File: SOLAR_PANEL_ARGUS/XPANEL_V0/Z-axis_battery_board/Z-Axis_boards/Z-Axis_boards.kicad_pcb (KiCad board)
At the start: 2 copper layers, 95.9 x 90.2 mm, 34 parts, among them J1 0530470810, Q1 BSS138, Q2 BSS138, Q3 MBT2222ADW1T1, Q4 BSS138, Q5 BSS138, Q6 MBT2222ADW1T1, U1 DRV8830DGQ

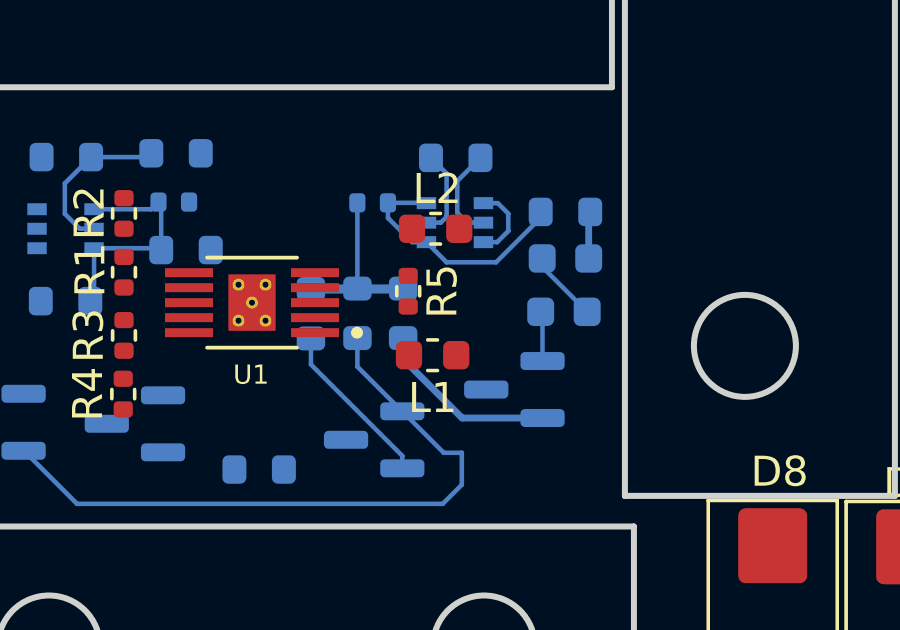
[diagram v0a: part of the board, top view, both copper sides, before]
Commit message: Started intial coil loop on first layer on Z-Axis board
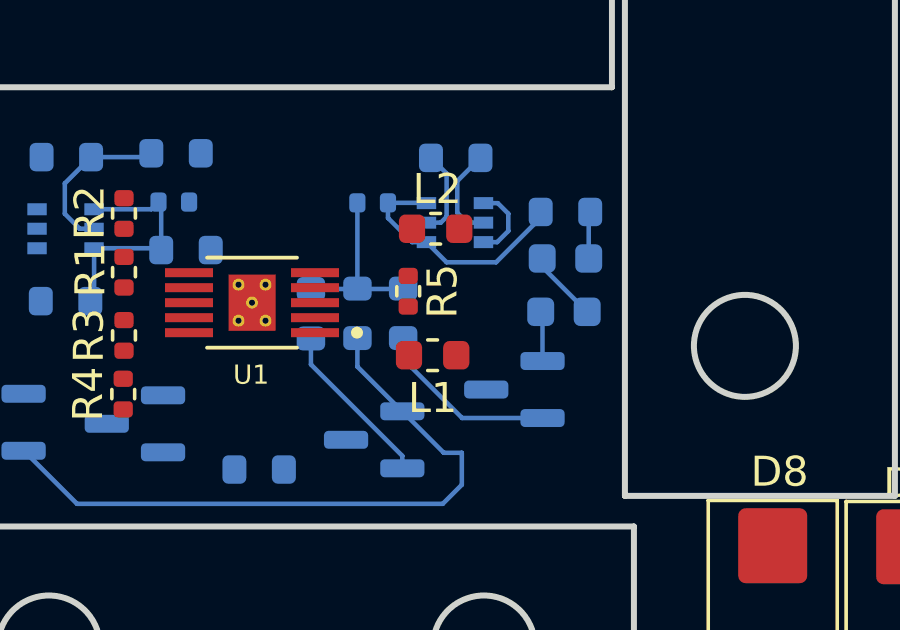
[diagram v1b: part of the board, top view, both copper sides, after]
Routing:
- net (no net): track 0.00 -> 7292.9 mm
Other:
- copper layers 2 -> 8

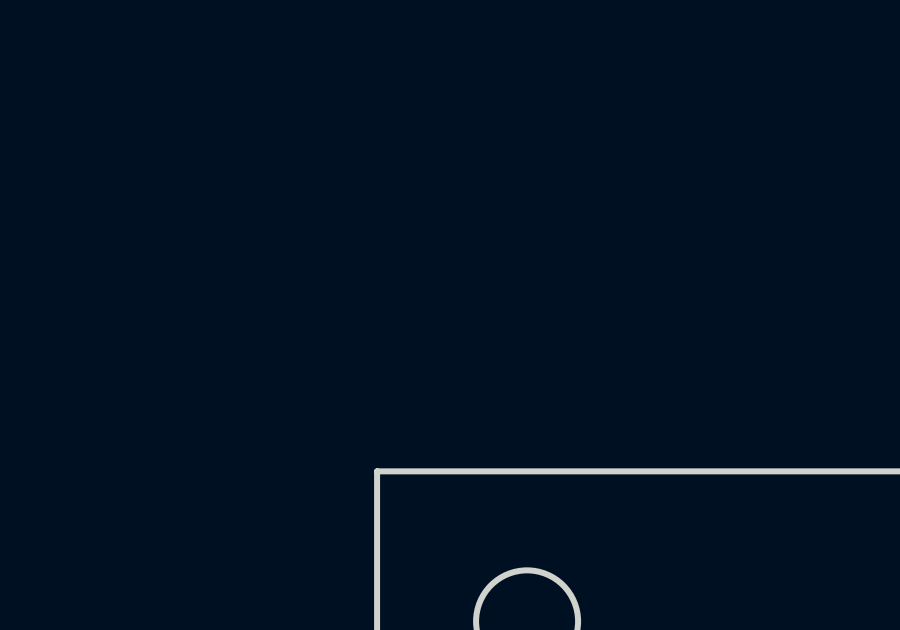
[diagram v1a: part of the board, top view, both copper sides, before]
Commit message: Added 52 loops of coil trace wiring on first 2 layers of z-axis battery board
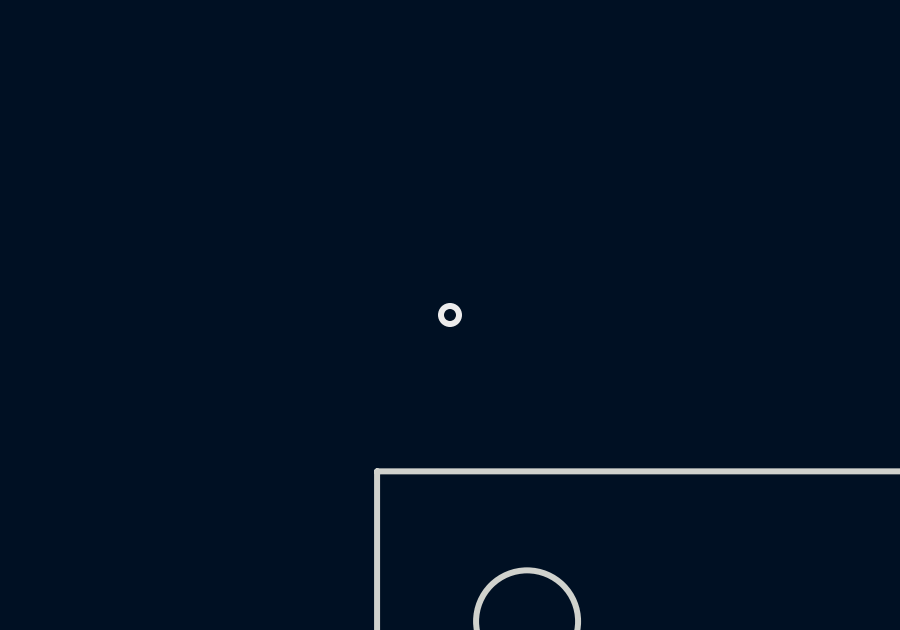
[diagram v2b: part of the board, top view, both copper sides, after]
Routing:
- net /coils: track 0.00 -> 31109.3 mm, vias 0 -> 1
- net (no net): track 7292.9 -> 0.00 mm

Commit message: completed z axis board
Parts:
- moved L2 5.68 mm to (158.7, 104.2)
- moved R5 4.74 mm to (162.1, 100.9)
- moved L1 4.44 mm to (160.4, 98.9)
- moved U1 0.57 mm to (152.6, 100.7)
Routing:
- net /coils: track 31109.3 -> 92567.8 mm, vias 1 -> 7
- net +3.3V: track 5.94 -> 100.7 mm, vias 0 -> 3
- net Net-(D7-K): track 0.00 -> 68.2 mm, vias 0 -> 1
- net GND: track 2.40 -> 63.6 mm, vias 0 -> 176
- net SCL1_b4iso: track 2.53 -> 44.9 mm, vias 0 -> 2
- net VBATT: track 0.00 -> 34.9 mm
- net Net-(Q1-S): track 8.52 -> 38.1 mm, vias 0 -> 2
- net Net-(Q5-G): track 1.67 -> 29.5 mm, vias 0 -> 2
- net Net-(Q2-G): track 1.60 -> 27.9 mm, vias 0 -> 3
- net SDA1_b4iso: track 0.00 -> 22.8 mm
- net SCL: track 8.30 -> 26.0 mm, vias 0 -> 2
- net Net-(Q4-G): track 6.16 -> 16.0 mm
- net Net-(Q4-S): track 5.49 -> 14.7 mm
- net Net-(U1-ISENSE): track 0.00 -> 7.41 mm
- net SDA: track 7.96 -> 13.7 mm, vias 0 -> 1
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- added copper zone on F.Cu, net GND
- added copper zone on In1.Cu, net GND
- added copper zone on In2.Cu, net GND
- added copper zone on In3.Cu, net GND
- added copper zone on In4.Cu, net GND
- added copper zone on In5.Cu, net GND
- added copper zone on In6.Cu, net GND
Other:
- outline, holes or cut-outs redrawn

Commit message: made changes to Z axis with new cutout
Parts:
- moved Q5 6.77 mm to (167.1, 106.4), turned to 90 degrees
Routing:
- net Net-(Q5-G): track 29.5 -> 40.4 mm
- net Net-(Q4-G): track 16.0 -> 23.0 mm
- net GND: track 63.6 -> 65.5 mm
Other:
- outline, holes or cut-outs redrawn
